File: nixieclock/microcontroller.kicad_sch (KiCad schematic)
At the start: 1 part, among them U8 STM32F058R8Tx

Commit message: mostly finalized pcb layout, silkscreen graphics, etc
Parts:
- removed U8: STM32F058R8Tx, Package_QFP:LQFP-64_10x10mm_P0.5mm, symbol MCU_ST_STM32F0:STM32F058R8Tx
- added BT1: Battery_Cell, Battery:BatteryHolder_Keystone_3000_1x12mm, symbol Device:Battery_Cell
- added C20, C21, C24: 100nF, Capacitor_SMD:C_0603_1608Metric_Pad1.05x0.95mm_HandSolder, symbol Device:C_Small
- added C22: 10nF, Capacitor_SMD:C_0603_1608Metric_Pad1.05x0.95mm_HandSolder, symbol Device:C_Small
- added C23: 1uF, Capacitor_SMD:C_0603_1608Metric_Pad1.05x0.95mm_HandSolder, symbol Device:C_Small
- added C25, C26, C27, C28: C_Small, symbol Device:C_Small
- added J2: Conn_ARM_JTAG_SWD_10, Connector_PinHeader_2.54mm:PinHeader_2x05_P2.54mm_Vertical_SMD, symbol Connector:Conn_ARM_JTAG_SWD_10
- added R13: ?, symbol Device:R_Small
- added R14: 10k, Resistor_SMD:R_0603_1608Metric_Pad1.05x0.95mm_HandSolder, symbol Device:R_Small
- added U8: STM32F051R4Tx, Package_QFP:LQFP-64_10x10mm_P0.5mm, symbol MCU_ST_STM32F0:STM32F051R4Tx
- added Y1: 8MHz, symbol Device:Crystal
- added Y2: 32.768kHz, symbol Device:Crystal
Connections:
- new net: C26.1, R13.2, Y1.2
- new net: R14.2, U8.60 (BOOT0)
- new net +3V3: C20.1, C21.1, C22.1, C23.1, J2.1 (VTref), U8.13 (VDDA), U8.32 (VDD), U8.64 (VDD)
- new net CLK: U8.21 (PA5)
- new net D: U8.23 (PA7)
- new net GND: BT1.2 (-), C20.2, C21.2, C22.2, C23.2, C24.2, C25.2, C26.2, C27.2, C28.2, J2.3 (GND), J2.5 (GND), J2.9 (GNDDetect), R14.1, U8.12 (VSSA), U8.31 (VSS), U8.63 (VSS)
- new net LCLK: U8.16 (PA2)
- new net OSC32_IN: U8.3 (PC14)
- new net OSC32_OUT: U8.4 (PC15)
- new net OSC_IN: C25.1, C27.1, U8.5 (PF0), Y1.1, Y2.1
- new net OSC_OUT: C28.1, R13.1, U8.6 (PF1), Y2.2
- new net SWDCLK: J2.4 (SWDCLK/TCK), U8.49 (PA14)
- new net SWDIO: J2.2 (SWDIO/TMS), U8.46 (PA13)
- new net VBAT: BT1.1 (+), U8.1 (VBAT)
- new net ~NRST: C24.1, J2.10 (~RESET~), U8.7 (NRST)
- new net ~OE: U8.14 (PA0)
- new net ~RES: U8.15 (PA1)
- new net ~SHDN: U8.17 (PA3)
- no-connect marks 0 -> 2
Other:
- note added: "BAT and Connectors"
- note added: "Decoupling Capacitors"
- note added: "Oscillators"
- note added: "See figures 13, and 24 of datasheet"
- company: (none) -> Bastian de Byl
- title: (none) -> Nixie Clock - Microcontroller

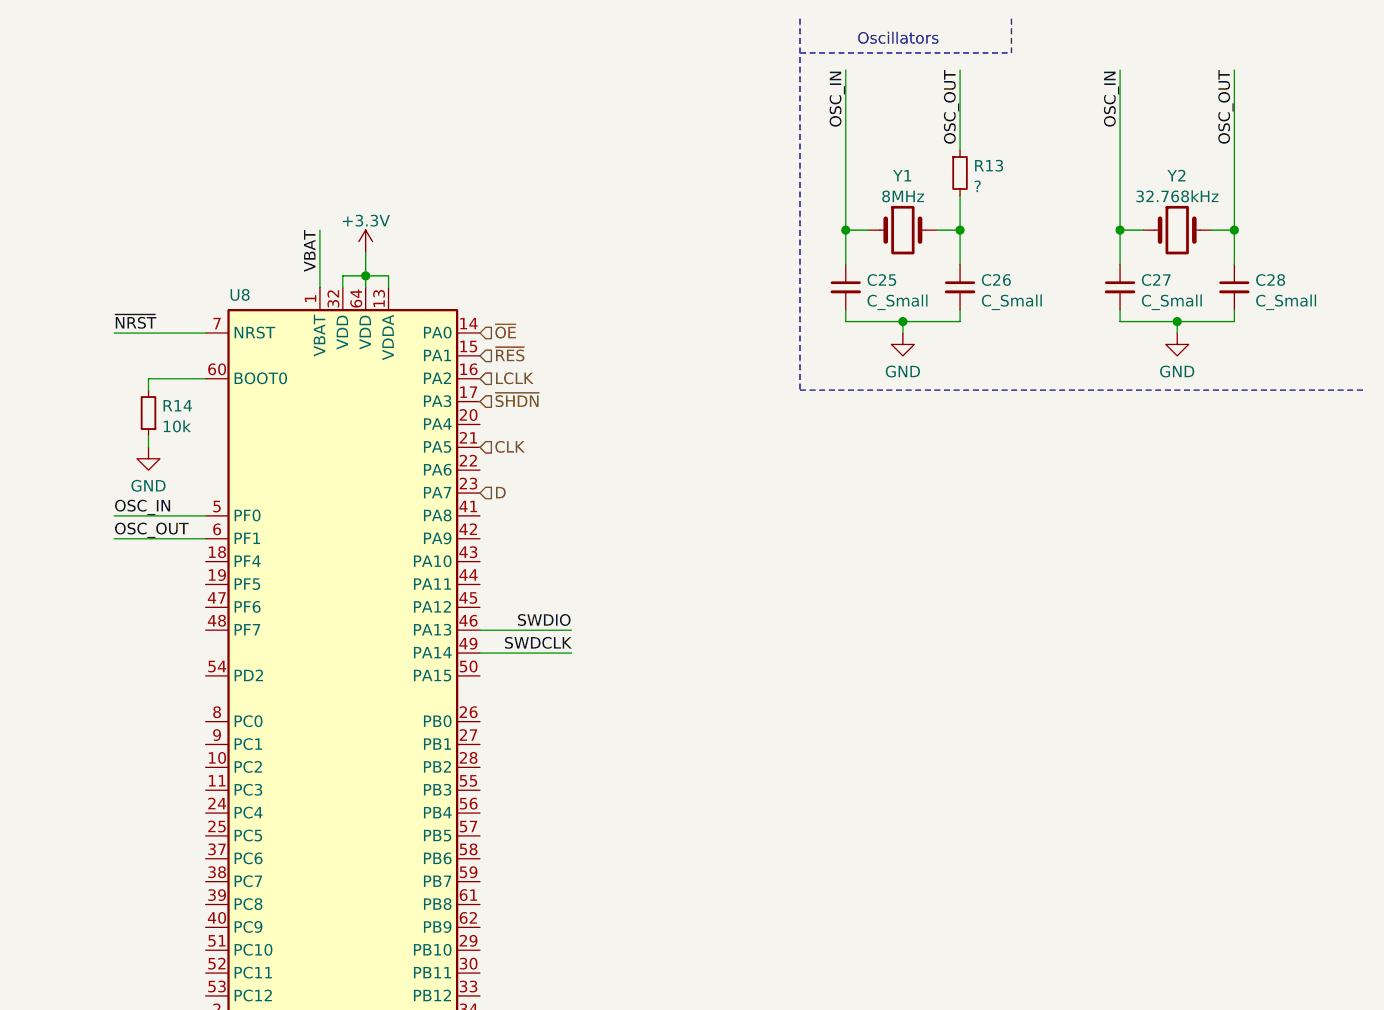
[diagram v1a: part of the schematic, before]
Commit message: finalized neon bulb design (todo: pcb jumpers)
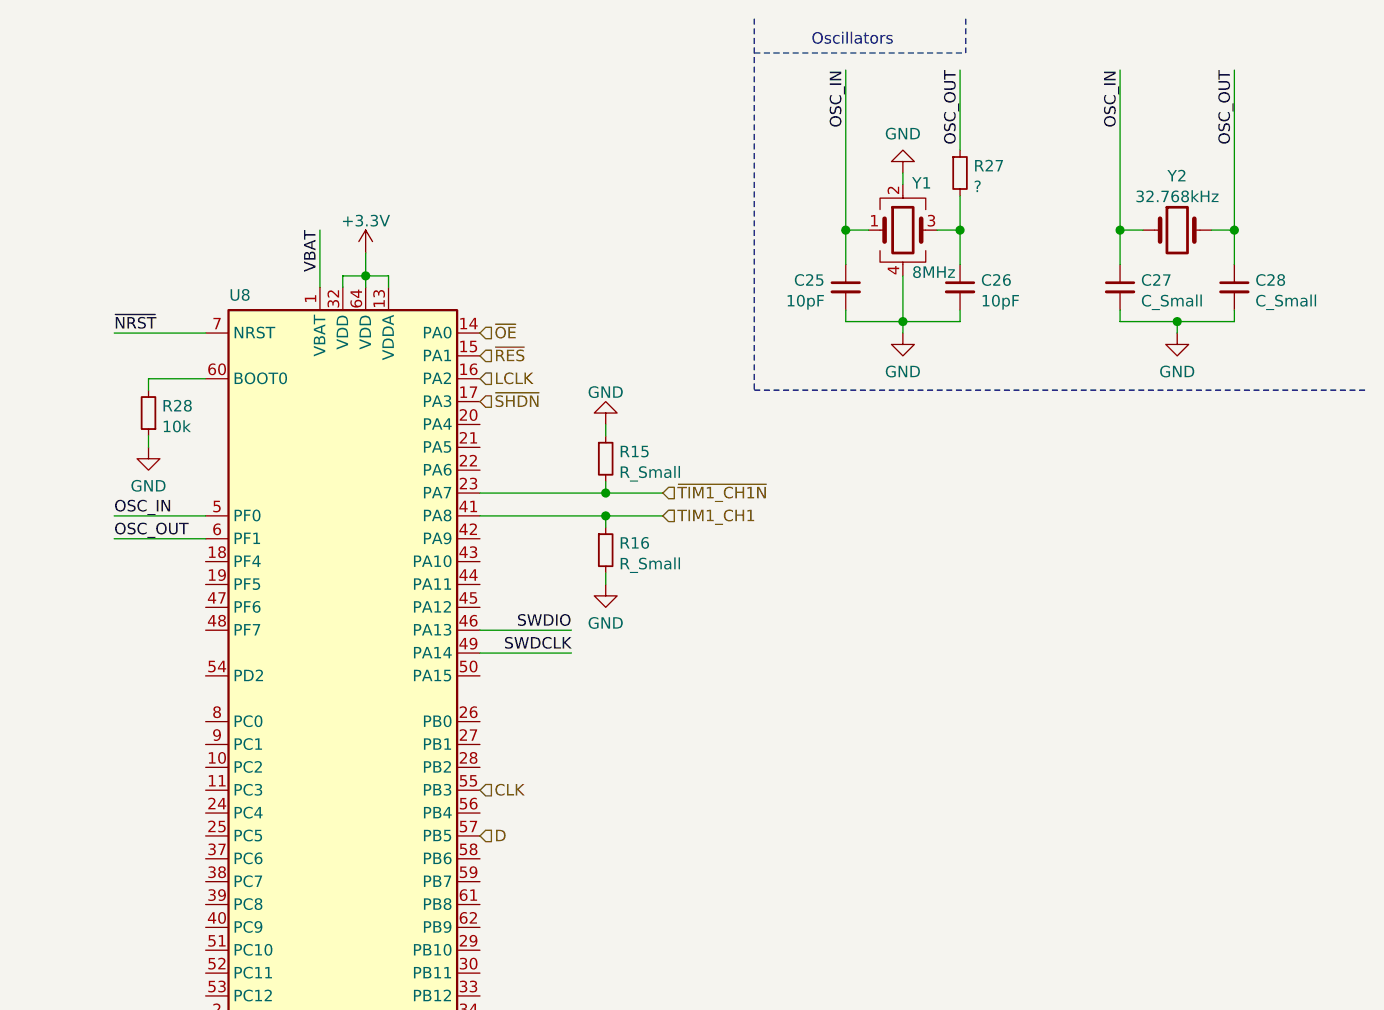
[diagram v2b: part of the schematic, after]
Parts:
- removed Y1: 8MHz, symbol Device:Crystal
- added R15, R16: R_Small, Resistor_SMD:R_0603_1608Metric_Pad1.05x0.95mm_HandSolder, symbol Device:R_Small
- added Y1: 8MHz, Crystal:Crystal_SMD_5032-4Pin_5.0x3.2mm, symbol Device:Crystal_GND24
- C25, C26: value C_Small -> 10pF; footprint (none) -> Capacitor_SMD:C_0603_1608Metric_Pad1.05x0.95mm_HandSolder
- R27: renamed from R13; footprint (none) -> Resistor_SMD:R_0603_1608Metric_Pad1.05x0.95mm_HandSolder
- renumbered R14 to R28
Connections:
- net CLK: now also U8.55 (PB3); no longer U8.21 (PA5)
- net D: now also U8.57 (PB5); no longer U8.23 (PA7)
- net GND: now also R15.1, R16.2, Y1.2, Y1.4
- net OSC_IN: now also Y1.1
- net at C26.1, R27.2: now also Y1.3
- net TIM1_CH1: now reaches U8.41 (PA8)
- net TIM1_CH1: now also R16.1
- new net ~TIM1_CH1N: R15.2, U8.23 (PA7)

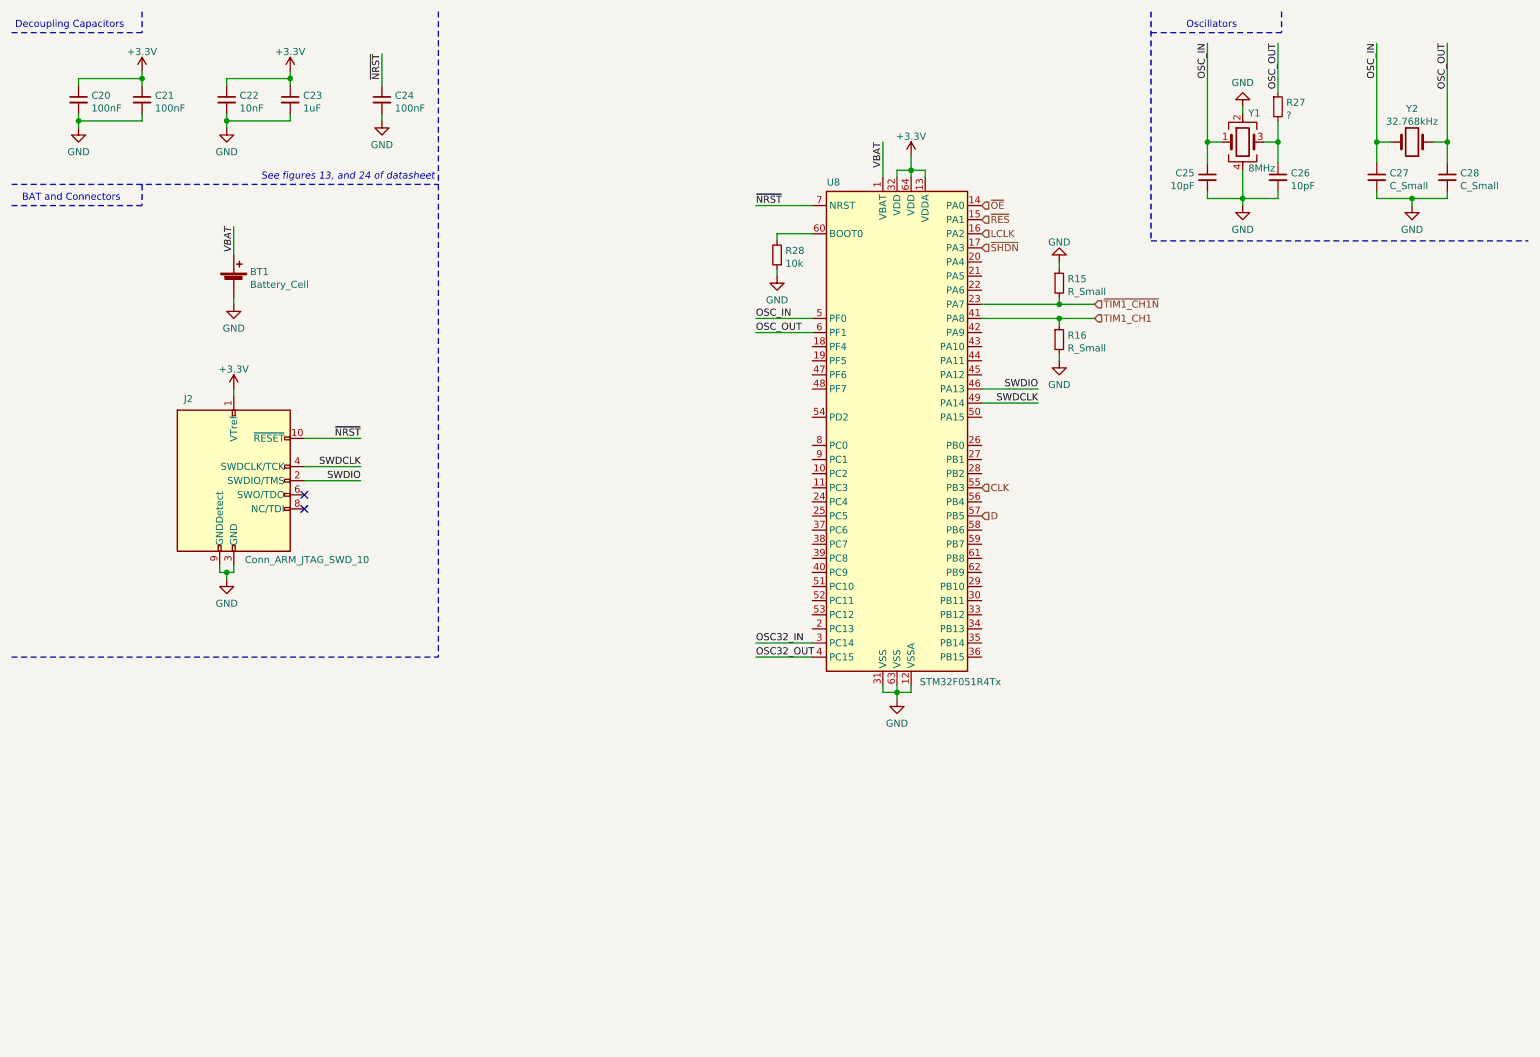
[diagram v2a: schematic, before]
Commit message: finalized layout, added encoder
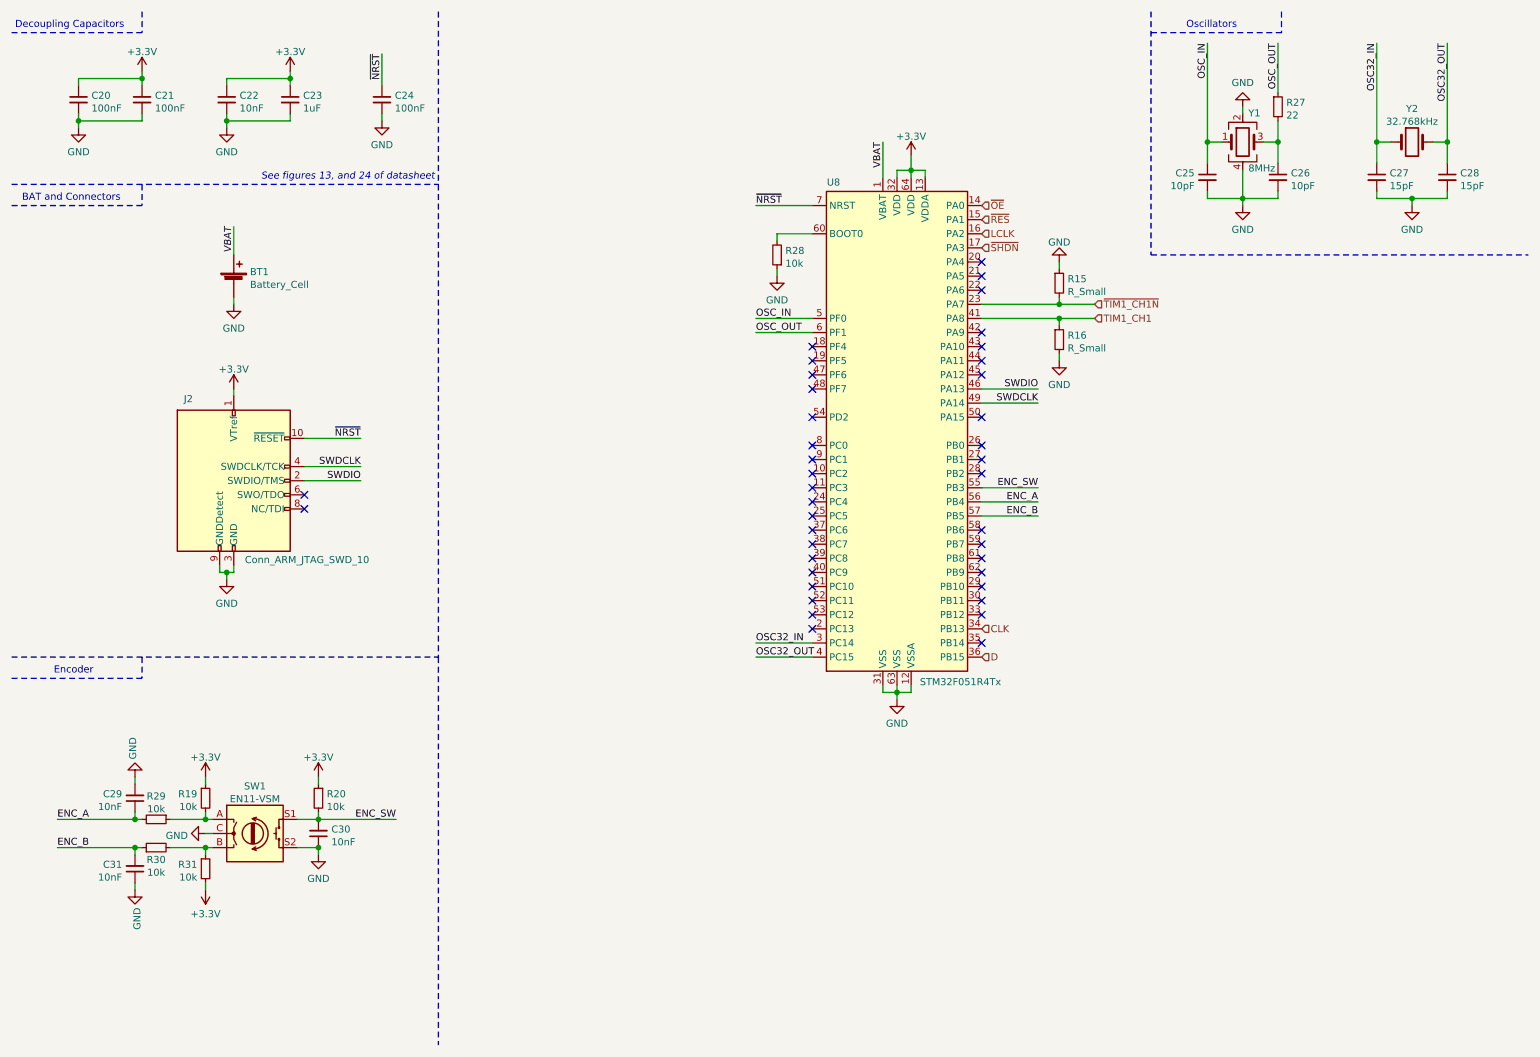
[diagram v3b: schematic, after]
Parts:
- added C29, C30, C31: 10nF, Capacitor_SMD:C_0603_1608Metric_Pad1.05x0.95mm_HandSolder, symbol Device:C_Small
- added R19, R20, R29, R30, R31: 10k, Resistor_SMD:R_0603_1608Metric_Pad1.05x0.95mm_HandSolder, symbol Device:R_Small
- added SW1: EN11-VSM, Personal:EN11-VSM1AF20, symbol Device:Rotary_Encoder_Switch
- C27, C28: value C_Small -> 15pF; footprint (none) -> Capacitor_SMD:C_0603_1608Metric_Pad1.05x0.95mm_HandSolder
- R27: value ? -> 22
- Y2: footprint (none) -> Crystal:Crystal_SMD_3215-2Pin_3.2x1.5mm
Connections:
- net +3V3: now also R19.1, R20.1, R31.2
- net CLK: now also U8.34 (PB13); no longer U8.55 (PB3)
- net D: now also U8.36 (PB15); no longer U8.57 (PB5)
- net GND: now also C29.2, C30.1, C31.1, SW1.C, SW1.S2
- net OSC32_IN: now also C27.1, Y2.1
- net OSC32_OUT: now also C28.1, Y2.2
- net OSC_IN: no longer C27.1, Y2.1
- net OSC_OUT: no longer C28.1, Y2.2
- net ENC_A: now reaches U8.56 (PB4)
- net ENC_A: now also C29.1, R29.2
- new net: R19.2, R29.1, SW1.A
- new net: R30.2, R31.1, SW1.B
- new net ENC_B: C31.2, R30.1, U8.57 (PB5)
- new net ENC_SW: C30.2, R20.2, SW1.S1, U8.55 (PB3)
- no-connect marks 2 -> 40
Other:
- note added: "Encoder"

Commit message: finalized design ready for quality check
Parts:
- added D4: LTST-C190GKT, LED_SMD:LED_0603_1608Metric_Pad1.05x0.95mm_HandSolder, symbol Device:LED_Small
- added R34: 1.2k, Resistor_SMD:R_0603_1608Metric_Pad1.05x0.95mm_HandSolder, symbol Device:R_Small
- BT1: footprint Battery:BatteryHolder_Keystone_3000_1x12mm -> Battery:BatteryHolder_MPD_BK912-1x2032
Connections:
- net ENC_A: now also U8.37 (PC6); no longer U8.56 (PB4)
- net ENC_B: now also U8.38 (PC7); no longer U8.57 (PB5)
- net ENC_SW: now also U8.39 (PC8); no longer U8.55 (PB3)
- net GND: now also R34.2
- net at U8.50 (PA15): now also D4.2 (A)
- new net: D4.1 (K), R34.1
- no-connect marks 40 -> 39
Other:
- note added: "(TIM3_CH1)"
- note added: "(TIM3_CH2)"
- note added: "MCU_OK"
- note added: "Microcontroller"
- moved on the sheet: R15, R16, R28, U8

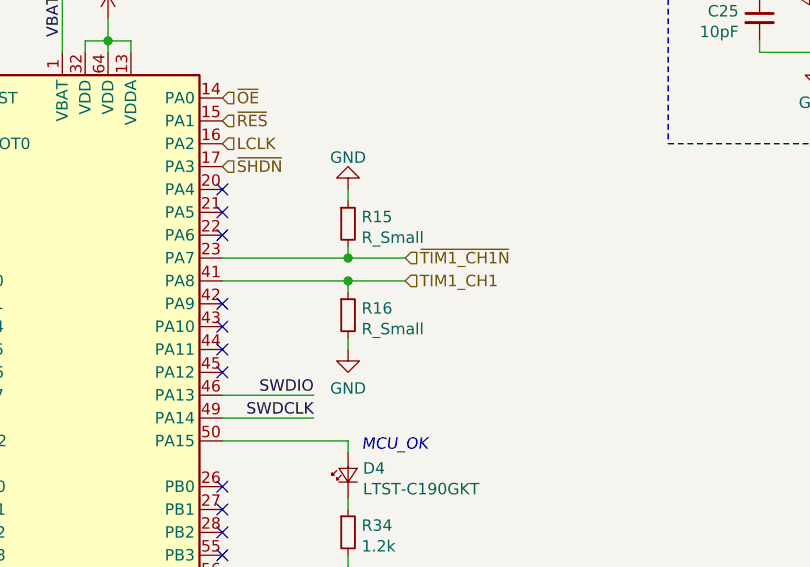
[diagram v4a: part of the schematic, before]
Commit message: finalized design, fixed USB C receptacle for hand soldering
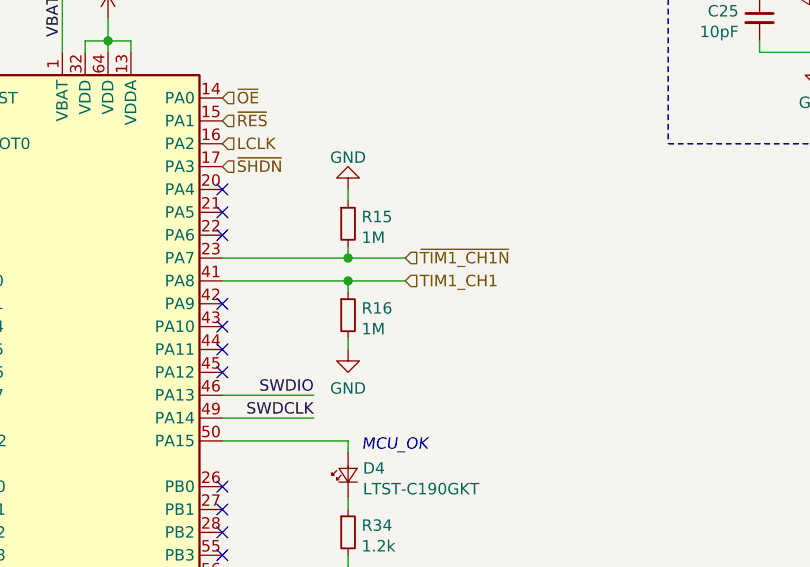
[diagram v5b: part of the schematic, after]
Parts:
- R15, R16: value R_Small -> 1M
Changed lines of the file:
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@@
       (effects (font (size 1.27 1.27)) (justify left))
     )
-    (property "Value" "R_Small" (id 1) (at 183.1087 66.3078 0)
+    (property "Value" "1M" (id 1) (at 183.1087 66.3078 0)
       (effects (font (size 1.27 1.27)) (justify left))
     )
@@
       (effects (font (size 1.27 1.27)) (justify left))
     )
-    (property "Value" "R_Small" (id 1) (at 183.1087 76.4678 0)
+    (property "Value" "1M" (id 1) (at 183.1087 76.4678 0)
       (effects (font (size 1.27 1.27)) (justify left))
     )
